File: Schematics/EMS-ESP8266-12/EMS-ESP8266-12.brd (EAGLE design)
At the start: 75.9 x 48.2 mm, 44 parts, among them IC1 LM393N, T1 BC547B, T2 BC547B

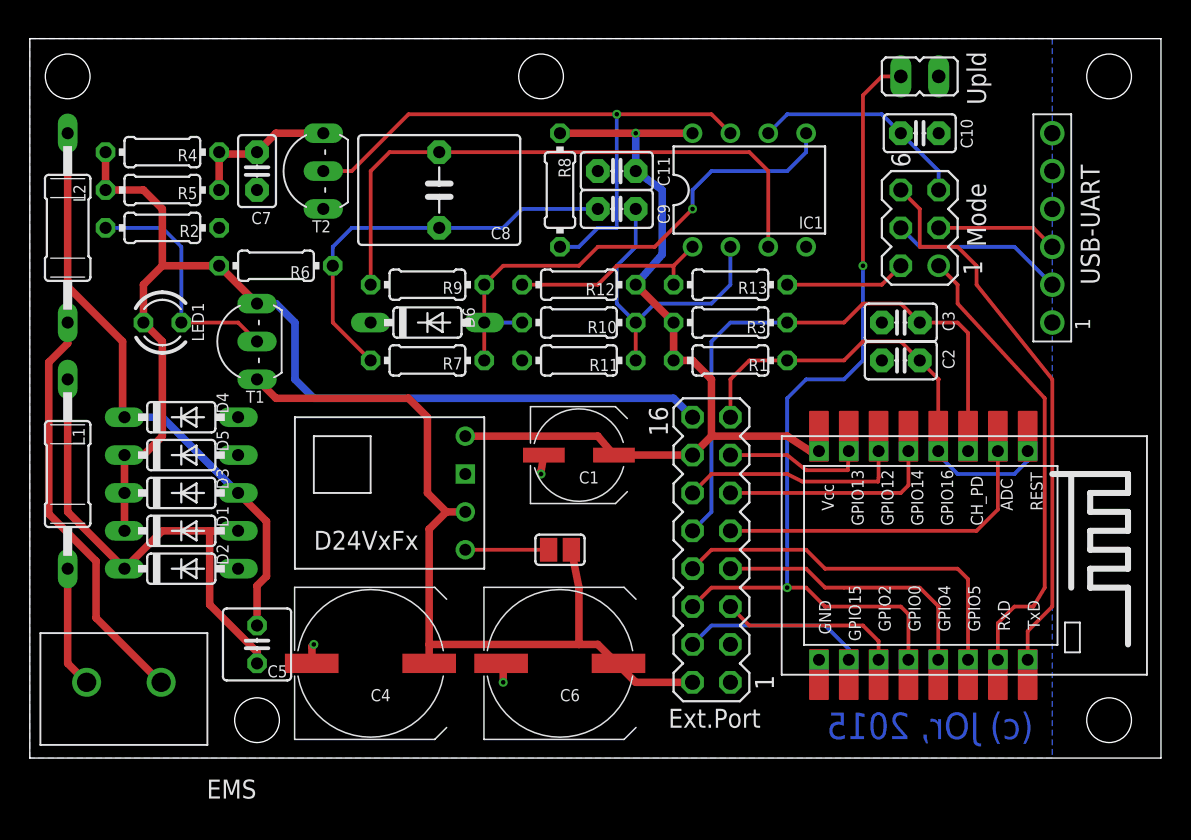
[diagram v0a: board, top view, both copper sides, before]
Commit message: EMS-ESP86266/12 Rev 1.0c
- Basiswiderstand R14 (10k) zur Strombegrenzung
- Package für T1,T2 in TO92 geändert
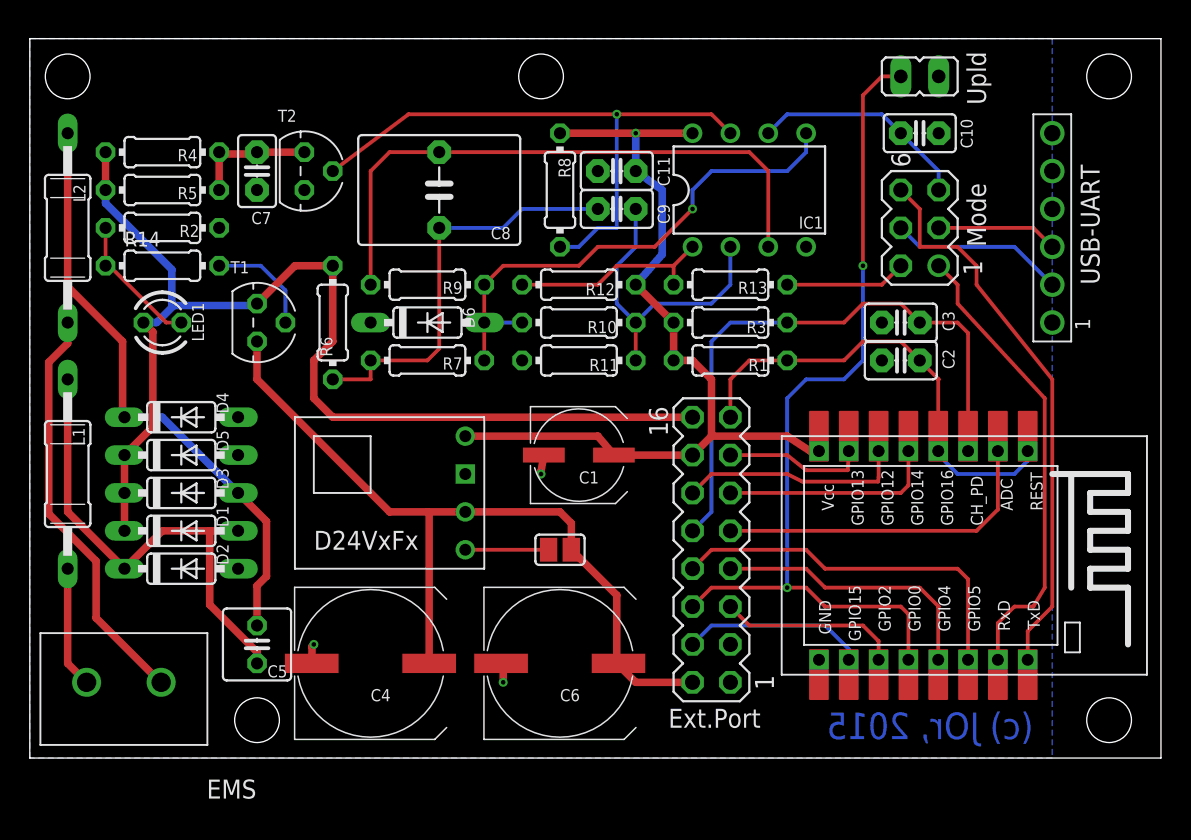
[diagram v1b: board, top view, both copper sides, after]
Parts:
- added R14: 10K, resistor:0204/7
- T1, T2: device transistor:TO92-EBC -> transistor:TO92
- moved R6 5.39 mm to (20.3, 29.2), turned to 90 degrees
- moved T1 1.80 mm to (15.2, 29.2), turned to 270 degrees
- turned T2 to 270 degrees
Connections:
- new net N$10: R14.2, T1.2
- net GND: now also T2.1; no longer T2.E
- net N$15: now also T2.2; no longer T2.B
- net N$17: now also R14.1; no longer T1.B
- net N$6: now also T2.3; no longer T2.C
- net UBUCK: now also T1.1; no longer T1.E
- net UEMS: now also T1.3; no longer T1.C
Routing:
- net N$10: track 0.00 -> 7.29 mm
- net N$17: track 16.3 -> 9.20 mm
- net UEMS: track 73.3 -> 76.8 mm
- net UBUCK: track 56.5 -> 54.1 mm
- net N$6: track 10.2 -> 8.36 mm
- net N$15: track 41.4 -> 40.4 mm
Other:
- board text added: "EMS-ESP8266/12 Rev 1.0c"
- board text removed: "EMS-ESP8266/12 Rev 1.0b"
